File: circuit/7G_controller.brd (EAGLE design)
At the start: 66.3 x 72 mm, 21 parts, among them Q1 32768Hz, T1 TPS1101D

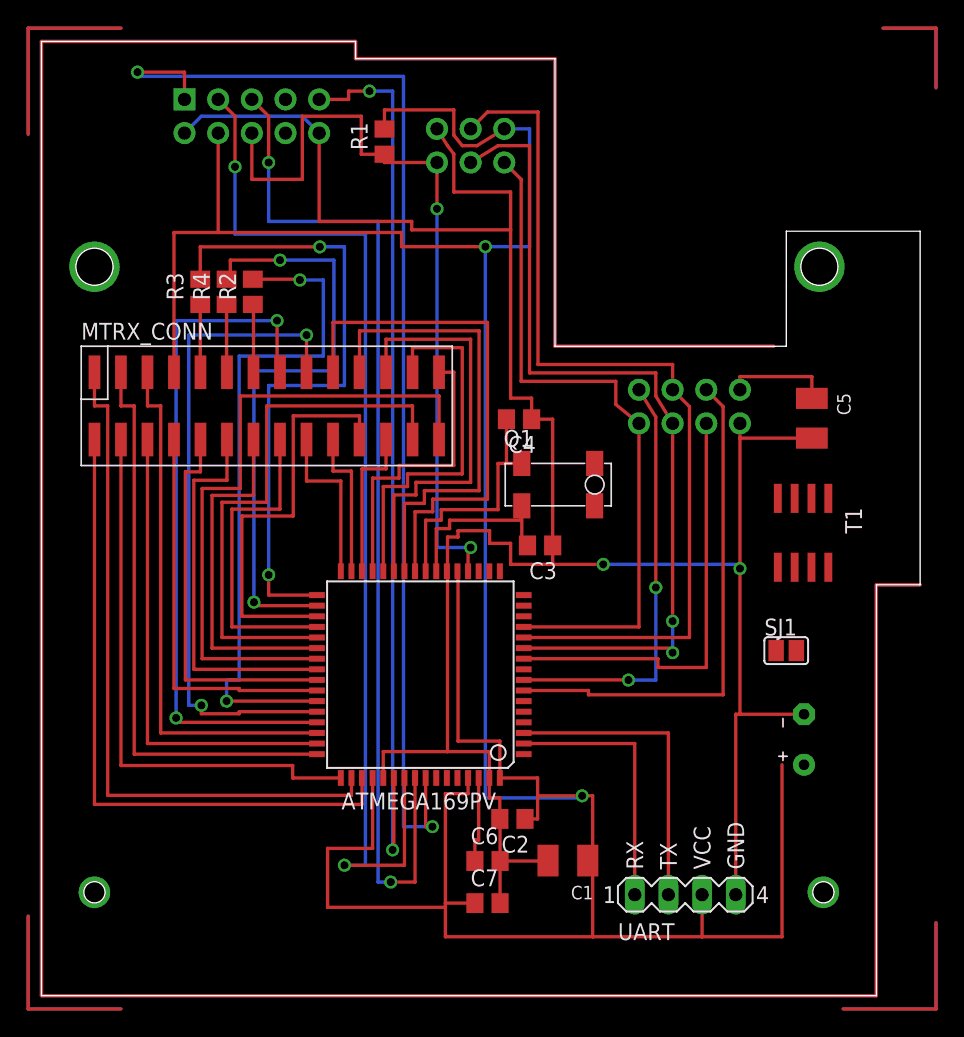
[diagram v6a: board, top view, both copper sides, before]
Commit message: renamed avr_serial -> avrdbg
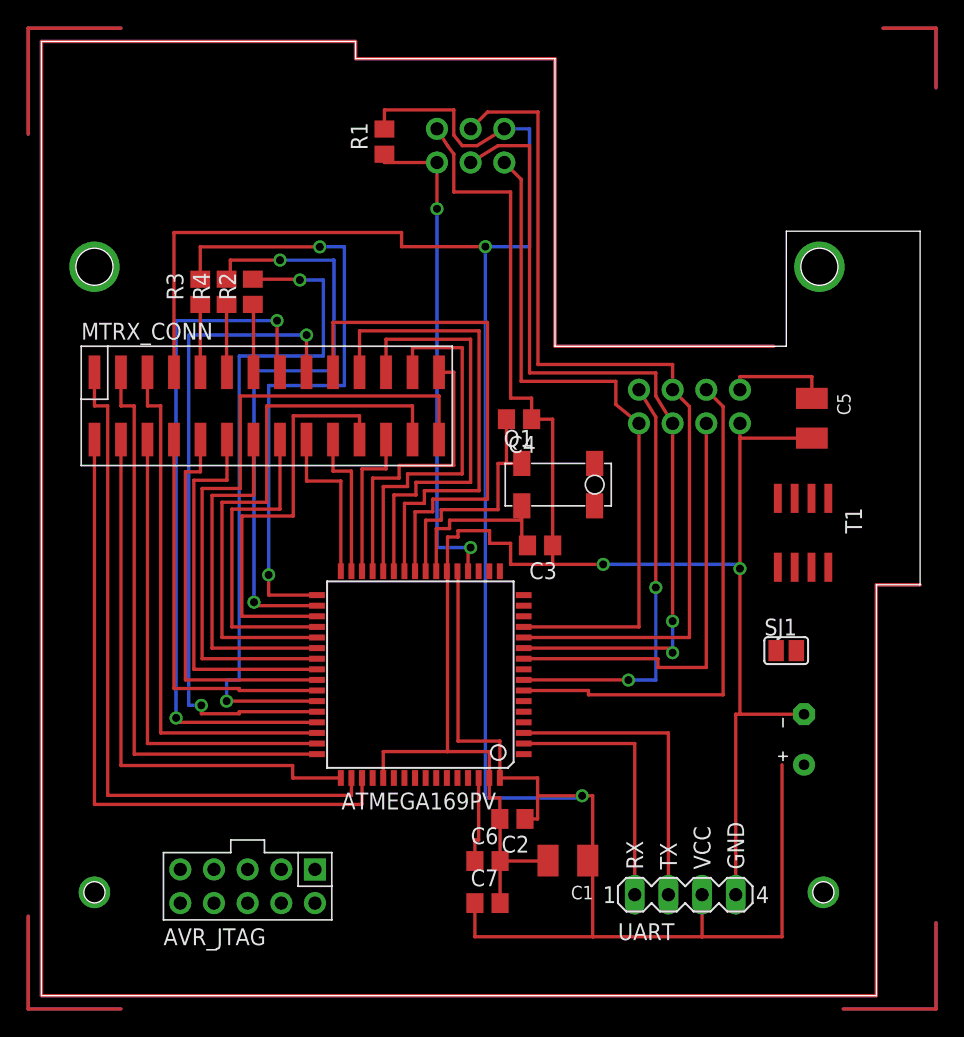
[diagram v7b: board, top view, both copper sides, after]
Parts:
- moved AVR_JTAG 58.1 mm to (15.6, 8.26), flipped to the top
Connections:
- net VCC: no longer ATMEGA169PV.61
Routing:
- net TCK: track 89.0 -> 0.00 mm, vias 2 -> 0
- net TDO: track 80.9 -> 0.00 mm, vias 2 -> 0
- net TMS: track 78.5 -> 0.00 mm, vias 2 -> 0
- net TDI: track 68.9 -> 0.00 mm, vias 2 -> 0
- net VCC: track 247.9 -> 202.8 mm
- net GND: track 187.3 -> 154.4 mm
- net RESET: track 59.3 -> 38.2 mm
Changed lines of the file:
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@@
 <element name="R3" library="rcl" package="R0805" value="470R" x="11.9825" y="53.1075" rot="R90"/>
 <element name="R4" library="rcl" package="R0805" value="470R" x="13.97" y="53.11" rot="R90"/>
-<element name="AVR_JTAG" library="KileParts" package="AVR-JTAG" value="AVR-JTAG" x="15.875" y="66.3575" rot="MR270"/>
+<element name="AVR_JTAG" library="KileParts" package="AVR-JTAG" value="AVR-JTAG" x="15.5575" y="8.255" rot="R270"/>
 <element name="C6" library="rcl" package="C0805" value="100nF" x="33.655" y="10.16"/>
 <element name="T1" library="KileParts" package="SO8" value="TPS1101D" x="57.4675" y="34.925" rot="R180"/>
@@
 <contactref element="AVR_ISP" pad="VCC"/>
 <contactref element="MTRX_CONN" pad="4"/>
-<contactref element="ATMEGA169PV" pad="61"/>
 <contactref element="UART" pad="+5V"/>
 <contactref element="AVR_JTAG" pad="P$4"/>
@@
 <via x="40.79875" y="15.08125" extent="1-16" drill="0.6" shape="square"/>
 <wire x1="40.79875" y1="15.08125" x2="37.43875" y2="15.08125" width="0.254" layer="1"/>
-<wire x1="10" y1="57.58375" x2="13.335" y2="57.58375" width="0.254" layer="1"/>
-<wire x1="13.335" y1="57.58375" x2="27.175" y2="57.58375" width="0.254" layer="1"/>
-<wire x1="24.99" y1="16.425" x2="24.99" y2="11.1125" width="0.254" layer="1"/>
-<wire x1="24.99" y1="11.1125" x2="21.59" y2="11.1125" width="0.254" layer="1"/>
-<wire x1="21.59" y1="11.1125" x2="21.59" y2="6.6675" width="0.254" layer="1"/>
-<wire x1="13.335" y1="65.0875" x2="13.335" y2="57.58375" width="0.254" layer="1"/>
+<wire x1="10" y1="57.58375" x2="27.175" y2="57.58375" width="0.254" layer="1"/>
 <wire x1="34.925" y1="65.405" x2="36.83" y2="65.405" width="0.254" layer="16"/>
 <wire x1="36.83" y1="65.405" x2="36.83" y2="56.515" width="0.254" layer="16"/>
@@
 <contactref element="SJ1" pad="1"/>
 <contactref element="C7" pad="1"/>
-<wire x1="30.48" y1="15.24" x2="30.48" y2="6.985" width="0.254" layer="1"/>
-<wire x1="30.48" y1="6.985" x2="30.48" y2="6.6675" width="0.254" layer="1"/>
-<wire x1="30.48" y1="6.6675" x2="21.59" y2="6.6675" width="0.254" layer="1"/>
-<wire x1="32.705" y1="6.985" x2="30.48" y2="6.985" width="0.254" layer="1"/>
-<wire x1="30.48" y1="4.445" x2="30.48" y2="6.6675" width="0.254" layer="1"/>
 <wire x1="49.8475" y1="4.445" x2="41.5925" y2="4.445" width="0.254" layer="1"/>
-<wire x1="41.5925" y1="4.445" x2="30.48" y2="4.445" width="0.254" layer="1"/>
 <wire x1="41.5925" y1="15.08125" x2="41.5925" y2="10.16" width="0.254" layer="1"/>
 <wire x1="41.5925" y1="10.16" x2="41.5925" y2="4.445" width="0.254" layer="1"/>
@@
 <wire x1="40.9575" y1="10.19125" x2="40.9575" y2="10.16" width="0.254" layer="1"/>
 <wire x1="40.9575" y1="10.16" x2="41.5925" y2="10.16" width="0.254" layer="1"/>
-<wire x1="30.48" y1="15.24" x2="32.19" y2="15.24" width="0.254" layer="1"/>
-<wire x1="32.19" y1="15.24" x2="32.19" y2="16.425" width="0.254" layer="1"/>
+<wire x1="41.5925" y1="4.445" x2="32.705" y2="4.445" width="0.254" layer="1"/>
+<wire x1="32.705" y1="4.445" x2="32.705" y2="6.985" width="0.254" layer="1"/>
 <wire x1="58.1025" y1="37.525" x2="58.13125" y2="45.0675" width="0" layer="19" extent="1-1"/>
 <wire x1="59.3725" y1="37.525" x2="58.1025" y2="37.525" width="0" layer="19" extent="1-1"/>
@@
 <wire x1="55.4355" y1="26.035" x2="56.8325" y2="37.525" width="0" layer="19" extent="1-1"/>
 <wire x1="55.88" y1="17.425" x2="55.4355" y2="26.035" width="0" layer="19" extent="1-1"/>
+<wire x1="24.99" y1="16.425" x2="31.4325" y2="19.20875" width="0" layer="19" extent="1-1"/>
+<wire x1="18.0975" y1="6.985" x2="24.99" y2="16.425" width="0" layer="19" extent="1-1"/>
 </signal>
 <signal name="GND">
@@
 <wire x1="52.705" y1="32.54375" x2="42.38625" y2="32.54375" width="0.254" layer="16"/>
 <via x="42.38625" y="32.54375" extent="1-16" drill="0.6" shape="square"/>
-<wire x1="35.40125" y1="60.6425" x2="35.40125" y2="57.785" width="0.254" layer="1"/>
-<wire x1="10.795" y1="65.0875" x2="12.065" y2="66.3575" width="0.254" layer="16"/>
-<wire x1="12.065" y1="66.3575" x2="19.685" y2="66.3575" width="0.254" layer="16"/>
-<wire x1="19.685" y1="66.3575" x2="20.955" y2="65.0875" width="0.254" layer="16"/>
-<wire x1="20.955" y1="58.42" x2="27.94" y2="58.42" width="0.254" layer="1"/>
-<wire x1="27.94" y1="58.42" x2="27.94" y2="57.785" width="0.254" layer="1"/>
-<wire x1="27.94" y1="57.785" x2="35.40125" y2="57.785" width="0.254" layer="1"/>
-<wire x1="20.955" y1="65.0875" x2="20.955" y2="58.42" width="0.254" layer="1"/>
 <contactref element="C5" pad="-"/>
 <contactref element="C6" pad="2"/>
@@
 <wire x1="38.57375" y1="32.54375" x2="38.57375" y2="33.9725" width="0.254" layer="1"/>
 <wire x1="42.38625" y1="32.54375" x2="38.57375" y2="32.54375" width="0.254" layer="1"/>
-<wire x1="35.40125" y1="57.785" x2="35.40125" y2="45.085" width="0.254" layer="1"/>
+<wire x1="35.40125" y1="60.6425" x2="35.40125" y2="45.085" width="0.254" layer="1"/>
 <wire x1="35.40125" y1="45.085" x2="36.98625" y2="45.085" width="0.254" layer="1"/>
 <wire x1="36.98625" y1="45.085" x2="36.98625" y2="43.4975" width="0.254" layer="1"/>
 <wire x1="58.13125" y1="42.0675" x2="55.5625" y2="37.525" width="0" layer="19" extent="1-1"/>
+<wire x1="20.6375" y1="6.985" x2="25.79" y2="16.425" width="0" layer="19" extent="1-1"/>
+<wire x1="10.4775" y1="6.985" x2="20.6375" y2="6.985" width="0" layer="19" extent="1-1"/>
 </signal>
 <signal name="MOSI">
@@
 <wire x1="29.845" y1="62.865" x2="25.88" y2="62.865" width="0.254" layer="1"/>
 <wire x1="25.88" y1="62.865" x2="25.88" y2="63.49" width="0.254" layer="1"/>
-<wire x1="15.875" y1="65.0875" x2="15.875" y2="61.595" width="0.254" layer="1"/>
-<wire x1="15.875" y1="61.595" x2="19.685" y2="61.595" width="0.254" layer="1"/>
-<wire x1="19.685" y1="61.595" x2="19.685" y2="66.3575" width="0.254" layer="1"/>
-<wire x1="19.685" y1="66.3575" x2="24.13" y2="66.3575" width="0.254" layer="1"/>
-<wire x1="24.13" y1="66.3575" x2="24.13" y2="63.49" width="0.254" layer="1"/>
-<wire x1="24.13" y1="63.49" x2="25.88" y2="63.49" width="0.254" layer="1"/>
+<wire x1="15.5575" y1="6.985" x2="32.19" y2="32.025" width="0" layer="19" extent="1-1"/>
 </signal>
 <signal name="TCK">
 <contactref element="ATMEGA169PV" pad="57"/>
 <contactref element="AVR_JTAG" pad="P$1"/>
-<wire x1="28.99" y1="16.425" x2="28.99" y2="12.75" width="0.254" layer="1"/>
-<wire x1="28.99" y1="12.75" x2="29.5" y2="12.75" width="0.254" layer="1"/>
-<via x="29.5" y="12.75" extent="1-16" drill="0.6" shape="square"/>
-<wire x1="29.5" y1="12.75" x2="27.3175" y2="12.75" width="0.254" layer="16"/>
-<wire x1="27.3175" y1="12.75" x2="27.3175" y2="69.365" width="0.254" layer="16"/>
-<via x="7.25" y="69.6825" extent="1-16" drill="0.6" shape="square"/>
-<wire x1="7.25" y1="69.6825" x2="10.795" y2="69.6825" width="0.254" layer="1"/>
-<wire x1="10.795" y1="67.6275" x2="10.795" y2="69.6825" width="0.254" layer="1"/>
-<wire x1="27.3175" y1="69.365" x2="7.25" y2="69.365" width="0.254" layer="16"/>
-<wire x1="7.25" y1="69.365" x2="7.25" y2="69.6825" width="0.254" layer="16"/>
+<wire x1="20.6375" y1="9.525" x2="28.99" y2="16.425" width="0" layer="19" extent="1-1"/>
 </signal>
 <signal name="TMS">
 <contactref element="ATMEGA169PV" pad="56"/>
 <contactref element="AVR_JTAG" pad="P$5"/>
-<wire x1="28.19" y1="16.425" x2="28.19" y2="8.5725" width="0.254" layer="1"/>
-<wire x1="28.19" y1="8.5725" x2="26.3525" y2="8.5725" width="0.254" layer="1"/>
-<via x="26.3525" y="8.5725" extent="1-16" drill="0.6" shape="square"/>
-<wire x1="26.3525" y1="8.5725" x2="25.4" y2="8.5725" width="0.254" layer="16"/>
-<wire x1="25.4" y1="8.5725" x2="25.4" y2="58.42" width="0.254" layer="16"/>
-<wire x1="25.4" y1="58.42" x2="17.145" y2="58.42" width="0.254" layer="16"/>
-<wire x1="17.145" y1="58.42" x2="17.145" y2="62.865" width="0.254" layer="16"/>
-<via x="17.145" y="62.865" extent="1-16" drill="0.6" shape="square"/>
-<wire x1="17.145" y1="62.865" x2="17.145" y2="66.3575" width="0.254" layer="1"/>
-<wire x1="17.145" y1="66.3575" x2="15.875" y2="67.6275" width="0.254" layer="1"/>
+<wire x1="15.5575" y1="9.525" x2="28.19" y2="16.425" width="0" layer="19" extent="1-1"/>
 </signal>
 <signal name="TDO">
 <contactref element="ATMEGA169PV" pad="55"/>
 <contactref element="AVR_JTAG" pad="P$3"/>
-<wire x1="27.39" y1="16.425" x2="27.39" y2="9.8425" width="0.254" layer="1"/>
-<wire x1="27.39" y1="9.8425" x2="22.86" y2="9.8425" width="0.254" layer="1"/>
-<via x="22.86" y="9.8425" extent="1-16" drill="0.6" shape="square"/>
-<wire x1="22.86" y1="9.8425" x2="24.4475" y2="9.8425" width="0.254" layer="16"/>
-<wire x1="24.4475" y1="9.8425" x2="24.4475" y2="57.4675" width="0.254" layer="16"/>
-<wire x1="24.4475" y1="57.4675" x2="14.605" y2="57.4675" width="0.254" layer="16"/>
-<wire x1="14.605" y1="57.4675" x2="14.605" y2="62.5475" width="0.254" layer="16"/>
-<via x="14.605" y="62.5475" extent="1-16" drill="0.6" shape="square"/>
-<wire x1="14.605" y1="62.5475" x2="14.605" y2="66.3575" width="0.254" layer="1"/>
-<wire x1="14.605" y1="66.3575" x2="13.335" y2="67.6275" width="0.254" layer="1"/>
+<wire x1="18.0975" y1="9.525" x2="27.39" y2="16.425" width="0" layer="19" extent="1-1"/>
 </signal>
 <signal name="TDI">
 <contactref element="ATMEGA169PV" pad="54"/>
 <contactref element="AVR_JTAG" pad="P$9"/>
-<via x="24.75" y="68.25" extent="1-16" drill="0.6" shape="square"/>
-<wire x1="24.75" y1="68.25" x2="26.5" y2="68.25" width="0.254" layer="16"/>
-<wire x1="26.5" y1="68.25" x2="26.5" y2="11" width="0.254" layer="16"/>
-<via x="26.5" y="11" extent="1-16" drill="0.6" shape="square"/>
-<wire x1="26.5" y1="11" x2="26.59" y2="11" width="0.254" layer="1"/>
-<wire x1="26.59" y1="11" x2="26.59" y2="16.425" width="0.254" layer="1"/>
-<wire x1="20.955" y1="67.6275" x2="23.1775" y2="67.6275" width="0.254" layer="1"/>
-<wire x1="23.1775" y1="67.6275" x2="23.1775" y2="68.25" width="0.254" layer="1"/>
-<wire x1="23.1775" y1="68.25" x2="24.75" y2="68.25" width="0.254" layer="1"/>
+<wire x1="10.4775" y1="9.525" x2="26.59" y2="16.425" width="0" layer="19" extent="1-1"/>
 </signal>
 <signal name="LEDSCRL">

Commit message: 
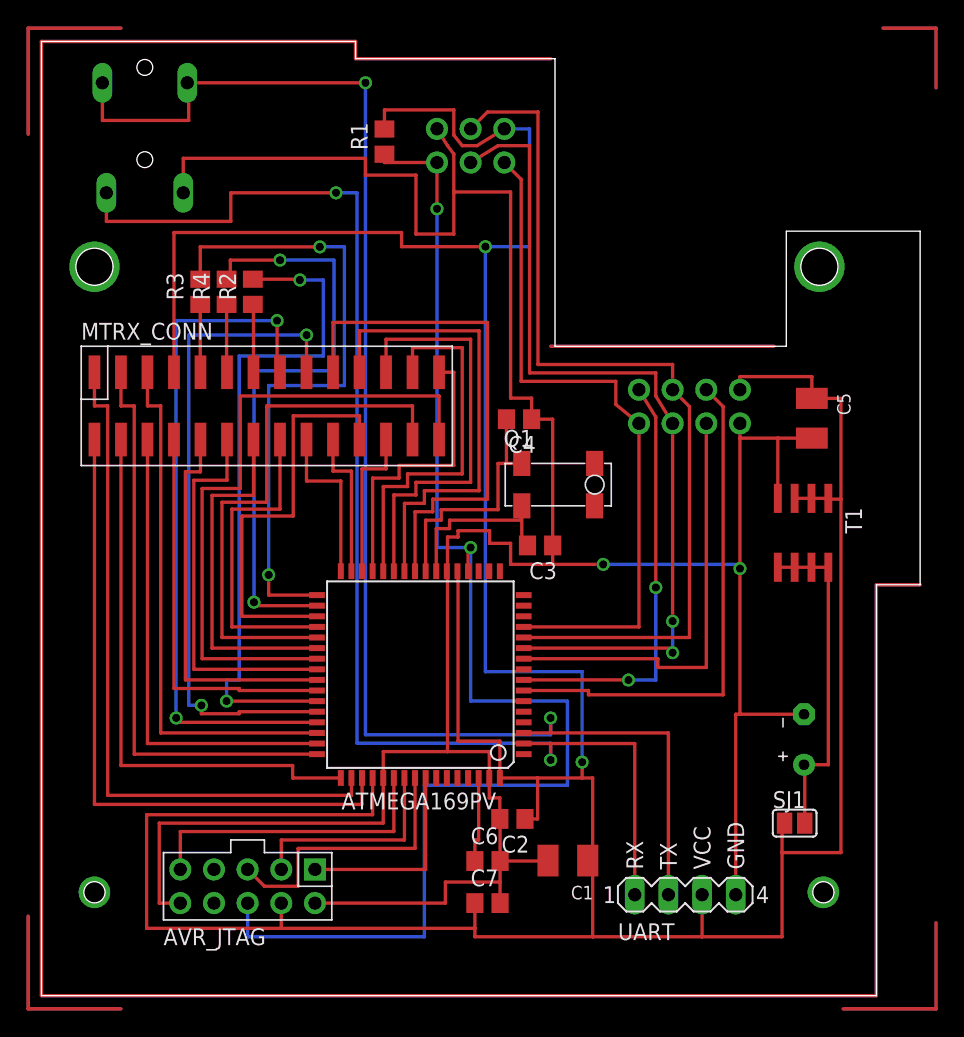
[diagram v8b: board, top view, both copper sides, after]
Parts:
- added DBG_JACK: JACK_FEMALE_3.5MMCHEAP, KileParts:JACK_CHEAP
- moved SJ1 13.0 mm to (56.8, 13.0)
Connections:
- net GND: now also DBG_JACK.1
- net N$29: now also DBG_JACK.4
- net N$30: now also DBG_JACK.2, DBG_JACK.3
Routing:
- net VCC: track 202.8 -> 297.8 mm
- net N$30: track 23.1 -> 114.4 mm, vias 0 -> 2
- net N$29: track 19.8 -> 101.7 mm, vias 0 -> 2
- net GND: track 154.4 -> 234.3 mm
- net RESET: track 38.2 -> 101.5 mm
- net N$19: track 247.6 -> 209.0 mm
- net N$1: track 247.6 -> 209.0 mm
- net N$4: track 0.00 -> 25.0 mm
- net TDI: track 0.00 -> 23.0 mm
- net TMS: track 0.00 -> 21.3 mm
- net N$7: track 0.00 -> 16.8 mm
- net N$5: track 0.00 -> 16.8 mm
- net TDO: track 0.00 -> 16.2 mm
- net TCK: track 0.00 -> 15.3 mm
